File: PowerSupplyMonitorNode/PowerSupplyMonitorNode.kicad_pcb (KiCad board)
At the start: 2 copper layers, 52 x 45 mm, 22 parts, among them J1 RJ45 PWR, J2 ADS1015, J3 VCC Sense, J4 HRPG, J5 A3, J6 A2, J7 A1, J8 A0, J9 ALERT, SW1 ADS_ADDR

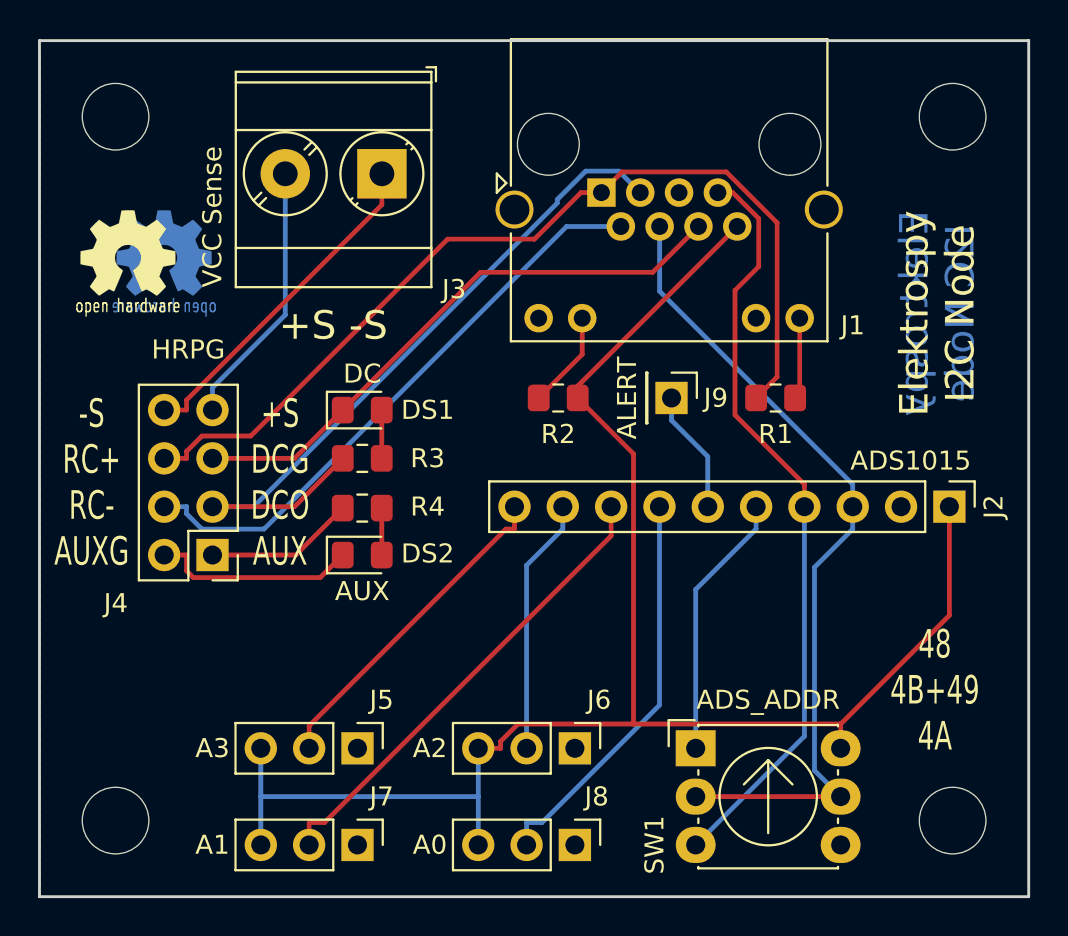
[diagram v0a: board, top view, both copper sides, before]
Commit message: added more pinout infos for i2c node to silkscreen
updated render of i2c node so show new silkscreen stuff
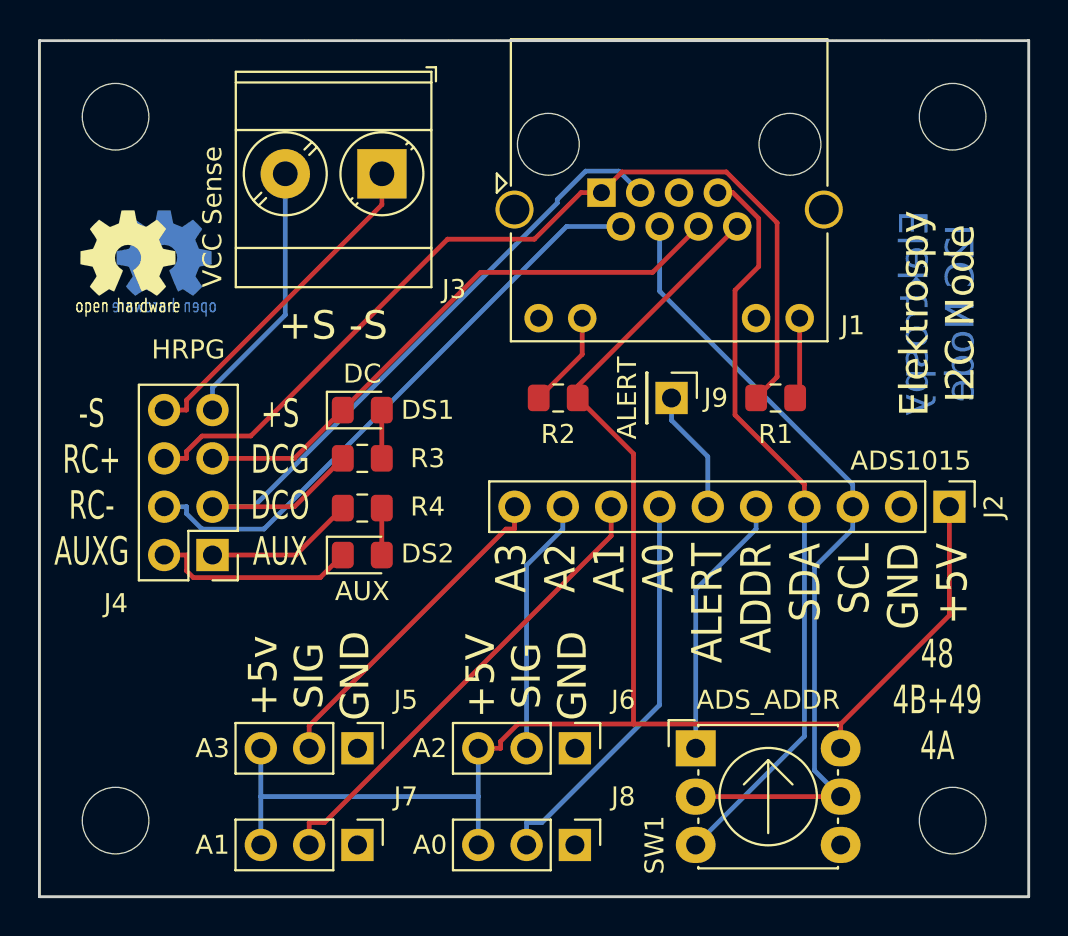
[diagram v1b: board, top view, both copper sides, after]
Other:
- board text added: "+5V SIG GND"
- board text added: "+5v SIG GND"
- board text added: "A3 A2 A1 A0 ALERT ADDR SDA SCL GND +5V"
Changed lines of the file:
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@@
   (general
     (thickness 1.6)
-    (drawings 10)
+    (drawings 13)
     (tracks 107)
     (zones 0)
@@
     (descr "Through hole straight pin header, 1x03, 2.54mm pitch, single row")
     (tags "Through hole pin header THT 1x03 2.54mm single row")
-    (fp_text reference J5 (at -2.54 -1.27) (layer F.SilkS)
+    (fp_text reference J5 (at -2.54 -2.54) (layer F.SilkS)
       (effects (font (size 1 1) (thickness 0.15)))
     )
@@
     (descr "Through hole straight pin header, 1x03, 2.54mm pitch, single row")
     (tags "Through hole pin header THT 1x03 2.54mm single row")
-    (fp_text reference J6 (at -2.54 -1.27) (layer F.SilkS)
+    (fp_text reference J6 (at -2.54 -2.54) (layer F.SilkS)
       (effects (font (size 1 1) (thickness 0.15)))
     )
@@
     (descr "Through hole straight pin header, 1x03, 2.54mm pitch, single row")
     (tags "Through hole pin header THT 1x03 2.54mm single row")
-    (fp_text reference J7 (at -2.54 -1.27) (layer F.SilkS)
+    (fp_text reference J7 (at -2.54 -2.54) (layer F.SilkS)
       (effects (font (size 1 1) (thickness 0.15)))
     )
@@
     (descr "Through hole straight pin header, 1x03, 2.54mm pitch, single row")
     (tags "Through hole pin header THT 1x03 2.54mm single row")
-    (fp_text reference J8 (at -2.54 -1.143) (layer F.SilkS)
+    (fp_text reference J8 (at -2.54 -2.54) (layer F.SilkS)
       (effects (font (size 1 1) (thickness 0.15)))
     )
@@
     (fp_line (start 2.16 -2.62) (end 2.16 -3.08) (layer B.Cu) (width 0.075))
   )
+  (gr_text "A3\nA2\nA1\nA0\nALERT\nADDR\nSDA\nSCL\nGND\n+5V" (at 152.4 65.405 90) (layer F.SilkS)
+    (effects (font (size 1.6 1.45) (thickness 0.15)) (justify right))
+  )
+  (gr_text "+5V\nSIG\nGND" (at 141.605 72.39 90) (layer F.SilkS)
+    (effects (font (size 1.5 1.5) (thickness 0.15)))
+  )
+  (gr_text "+5v\nSIG\nGND" (at 130.175 72.39 90) (layer F.SilkS)
+    (effects (font (size 1.5 1.5) (thickness 0.15)))
+  )
   (gr_text "Elektrospy\nI2C Node" (at 163.195 53.34 90) (layer B.Cu)
     (effects (font (size 1.5 1.5) (thickness 0.3)) (justify mirror))
@@
     (effects (font (size 1.5 1.5) (thickness 0.3)))
   )
-  (gr_text "48\n4B+49\n4A" (at 163.068 73.152) (layer F.SilkS)
+  (gr_text "48\n4B+49\n4A" (at 163.195 73.66) (layer F.SilkS)
     (effects (font (size 1.5 1) (thickness 0.15)))
   )

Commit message: added minimal readme
added many vias for ground front and back plane
updated 3d render of i2c hub pcb
updated gerber archive files
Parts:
- SW1: value ADS_ADDR -> ADS-ADDR
- moved SW1 8.43 mm to (157.2, 81.3), turned to 180 degrees
- turned R1 to 180 degrees
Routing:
- net /ADDR: track 14.0 -> 23.4 mm
- net /SDA: track 40.0 -> 33.8 mm
- net /SCL: track 43.2 -> 38.5 mm
- net /RC+: track 49.4 -> 52.2 mm
- net +5V: track 87.3 -> 89.0 mm
- net /A0: track 21.1 -> 22.6 mm
- net Net-(J1-Pad12): track 4.29 -> 5.14 mm
- net /DC_OK: track 38.3 -> 39.0 mm
- net /-S: track 17.8 -> 17.2 mm

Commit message: updated readme and license file
added datasheet for ads1015
added datasheet for pca9685
added foto of gy-712 30a sensor
added small changes to pcbs
updated 3d render of pcbs
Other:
- board text added: "4A 49+4B 48"
- board text removed: "48 4B+49 4A"
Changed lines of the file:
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@@
     (effects (font (size 1.5 1.5) (thickness 0.3)))
   )
-  (gr_text "48\n4B+49\n4A" (at 163.195 73.66) (layer F.SilkS)
+  (gr_text "4A\n49+4B\n48\n" (at 163.195 73.66) (layer F.SilkS)
     (effects (font (size 1.5 1) (thickness 0.15)))
   )
@@
   (segment (start 122.555 67.183) (end 122.936 67.564) (width 0.25) (layer F.Cu) (net 3))
   (segment (start 133.994 63.5715) (end 133.994 66.04) (width 0.25) (layer F.Cu) (net 4))
-  (segment (start 131.944 60.96) (end 129.404 63.5) (width 0.25) (layer F.Cu) (net 6))
-  (segment (start 129.404 63.5) (end 125.095 63.5) (width 0.25) (layer F.Cu) (net 6))
-  (segment (start 158.75 63.5) (end 158.75 62.3247) (width 0.25) (layer B.Cu) (net 10))
-  (segment (start 158.75 62.3247) (end 148.6 52.1747) (width 0.25) (layer B.Cu) (net 10))
-  (segment (start 148.6 52.1747) (end 148.6 48.77) (width 0.25) (layer B.Cu) (net 10))
-  (segment (start 127.635 78.74) (end 127.635 76.2) (width 0.25) (layer B.Cu) (net 11))
-  (segment (start 127.635 81.28) (end 127.635 78.74) (width 0.25) (layer B.Cu) (net 11))
-  (segment (start 139.065 78.74) (end 127.635 78.74) (width 0.25) (layer B.Cu) (net 11))
-  (segment (start 139.065 78.74) (end 139.065 76.2) (width 0.25) (layer B.Cu) (net 11))
-  (segment (start 139.065 81.28) (end 139.065 78.74) (width 0.25) (layer B.Cu) (net 11))
-  (segment (start 152.68 48.77) (end 144.29 57.16) (width 0.25) (layer F.Cu) (net 11))
-  (segment (start 144.29 57.16) (end 144.29 57.785) (width 0.25) (layer F.Cu) (net 11))
   (segment (start 155.72 57.785) (end 155.96 57.545) (width 0.25) (layer F.Cu) (net 5))
   (segment (start 155.72 57.785) (end 158.496 55.009) (width 0.25) (layer F.Cu) (net 5))
@@
   (segment (start 127.1981 59.69) (end 123.952 59.69) (width 0.25) (layer F.Cu) (net 5))
   (segment (start 123.952 59.69) (end 122.682 60.96) (width 0.25) (layer F.Cu) (net 5))
+  (segment (start 131.944 60.96) (end 129.404 63.5) (width 0.25) (layer F.Cu) (net 6))
+  (segment (start 129.404 63.5) (end 125.095 63.5) (width 0.25) (layer F.Cu) (net 6))
   (segment (start 147.574 46.736) (end 147.574 46.984) (width 0.25) (layer B.Cu) (net 6))
   (segment (start 127.762 63.5) (end 143.764 47.498) (width 0.25) (layer B.Cu) (net 6))
@@
   (segment (start 146.56 48.77) (end 143.7103 48.77) (width 0.25) (layer B.Cu) (net 9))
   (segment (start 143.7103 48.77) (end 127.7103 64.77) (width 0.25) (layer B.Cu) (net 9))
+  (segment (start 158.75 63.5) (end 158.75 62.3247) (width 0.25) (layer B.Cu) (net 10))
+  (segment (start 158.75 62.3247) (end 148.6 52.1747) (width 0.25) (layer B.Cu) (net 10))
+  (segment (start 148.6 52.1747) (end 148.6 48.77) (width 0.25) (layer B.Cu) (net 10))
   (segment (start 158.526 81.28) (end 157.226 81.28) (width 0.25) (layer B.Cu) (net 10))
   (segment (start 159.258 80.548) (end 158.526 81.28) (width 0.25) (layer B.Cu) (net 10))
   (segment (start 158.75 63.5) (end 159.258 64.008) (width 0.25) (layer B.Cu) (net 10))
   (segment (start 159.258 64.008) (end 159.258 80.548) (width 0.25) (layer B.Cu) (net 10))
+  (segment (start 127.635 78.74) (end 127.635 76.2) (width 0.25) (layer B.Cu) (net 11))
+  (segment (start 127.635 81.28) (end 127.635 78.74) (width 0.25) (layer B.Cu) (net 11))
+  (segment (start 139.065 78.74) (end 127.635 78.74) (width 0.25) (layer B.Cu) (net 11))
+  (segment (start 139.065 78.74) (end 139.065 76.2) (width 0.25) (layer B.Cu) (net 11))
+  (segment (start 139.065 81.28) (end 139.065 78.74) (width 0.25) (layer B.Cu) (net 11))
+  (segment (start 152.68 48.77) (end 144.29 57.16) (width 0.25) (layer F.Cu) (net 11))
+  (segment (start 144.29 57.16) (end 144.29 57.785) (width 0.25) (layer F.Cu) (net 11))
   (segment (start 149.098 81.28) (end 149.606 81.28) (width 0.25) (layer F.Cu) (net 11))
   (segment (start 146.812 78.994) (end 149.098 81.28) (width 0.25) (layer F.Cu) (net 11))

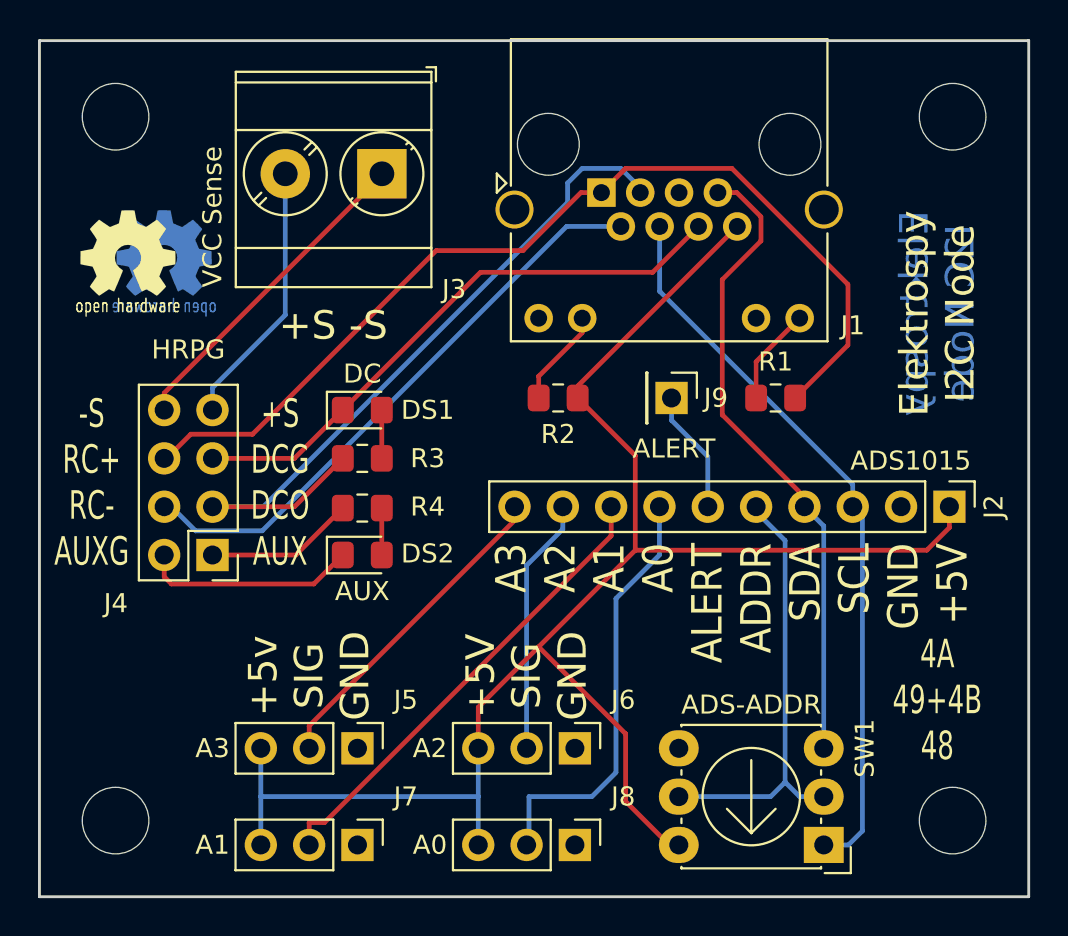
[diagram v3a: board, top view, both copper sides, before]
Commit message: fixed pcb errors
swapped gnd and vcc pin of 4 position switch to fix first two addresses
added custom 3d model for 4 position switch as step file
added custom library for 4 position switch
fixed routing of feedback signal lines (dc0-dc5)
removed double current limiting led resistors
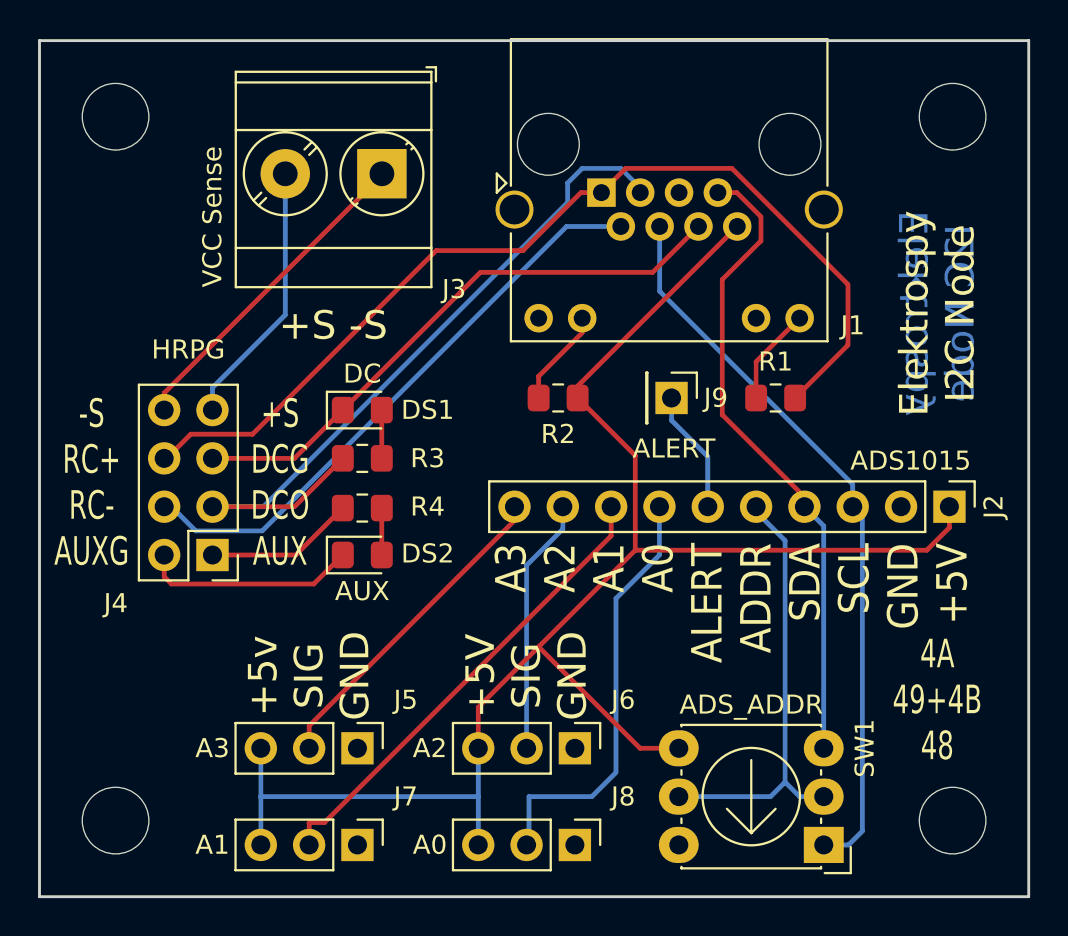
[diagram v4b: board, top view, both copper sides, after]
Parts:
- removed G***: LOGO, w_logo:Logo_silk_OSHW_6x6mm
- removed G***: LOGO, w_logo:Logo_copper_OSHW_6x6mm
- SW1: value ADS-ADDR -> ADS_ADDR; footprint Button_Switch_THT:Nidec_Copal_SH-7010C -> i2cNode:CTS_ 220AD_0
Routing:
- net +5V: track 89.0 -> 84.8 mm
